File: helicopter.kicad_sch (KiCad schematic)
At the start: 15 parts, among them J1 Conn_01x06, SW1 Tactswitch, U1 STM32L4P5RET6, Y1 16MHz

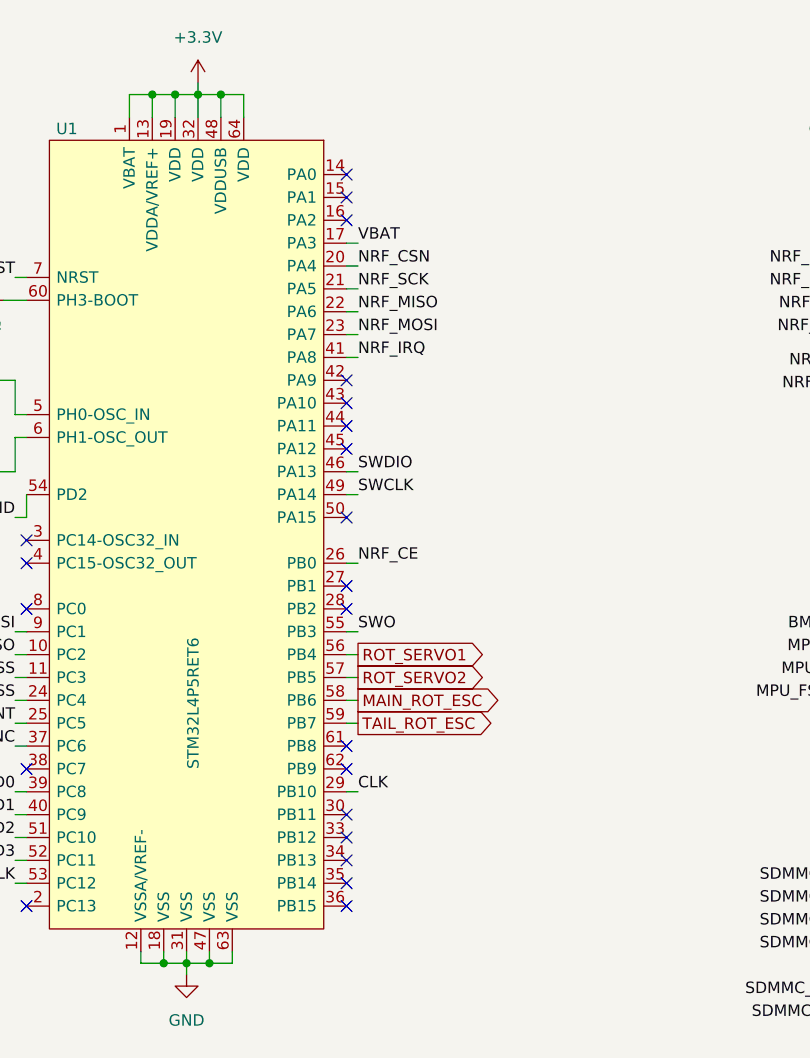
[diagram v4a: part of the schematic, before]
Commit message: Add external UART and I2C connectors
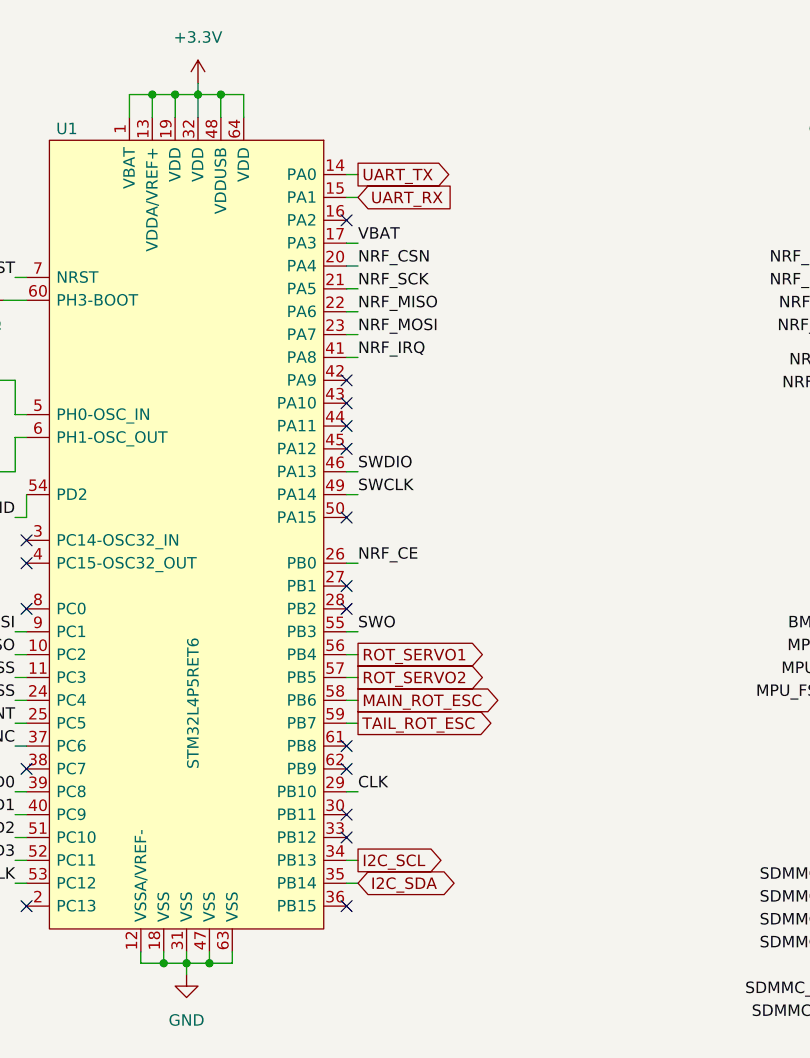
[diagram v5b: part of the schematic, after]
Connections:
- net UART_TX: now reaches U1.14 (PA0)
- net UART_RX: now reaches U1.15 (PA1)
- net I2C_SCL: now reaches U1.34 (PB13)
- net I2C_SDA: now reaches U1.35 (PB14)
- no-connect marks 22 -> 18
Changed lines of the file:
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@@
   (no_connect (at 130.81 96.52))
   (no_connect (at 166.37 81.28))
-  (no_connect (at 166.37 55.88))
   (no_connect (at 166.37 137.16))
   (no_connect (at 130.81 99.06))
   (no_connect (at 166.37 101.6))
-  (no_connect (at 166.37 58.42))
   (no_connect (at 166.37 86.36))
   (no_connect (at 166.37 129.54))
   (no_connect (at 166.37 60.96))
   (no_connect (at 130.81 137.16))
-  (no_connect (at 166.37 134.62))
   (no_connect (at 166.37 104.14))
-  (no_connect (at 166.37 132.08))
   (no_connect (at 166.37 127))
   (wire (pts (xy 107.95 78.74) (xy 111.76 78.74))
@@
     (stroke (width 0) (type default) (color 0 0 0 0))
   )
+  (wire (pts (xy 166.37 55.88) (xy 167.64 55.88))
+    (stroke (width 0) (type default) (color 0 0 0 0))
+  )
   (wire (pts (xy 76.2 128.27) (xy 67.31 128.27))
     (stroke (width 0) (type default) (color 0 0 0 0))
@@
     (stroke (width 0) (type default) (color 0 0 0 0))
   )
+  (wire (pts (xy 167.64 132.08) (xy 166.37 132.08))
+    (stroke (width 0) (type default) (color 0 0 0 0))
+  )
   (wire (pts (xy 129.54 129.54) (xy 130.81 129.54))
     (stroke (width 0) (type default) (color 0 0 0 0))
@@
     (stroke (width 0) (type default) (color 0 0 0 0))
   )
+  (wire (pts (xy 167.64 134.62) (xy 166.37 134.62))
+    (stroke (width 0) (type default) (color 0 0 0 0))
+  )
   (wire (pts (xy 251.46 44.45) (xy 252.73 44.45))
     (stroke (width 0) (type default) (color 0 0 0 0))
@@
     (stroke (width 0) (type default) (color 0 0 0 0))
   )
+  (wire (pts (xy 166.37 58.42) (xy 167.64 58.42))
+    (stroke (width 0) (type default) (color 0 0 0 0))
+  )
   (wire (pts (xy 148.59 143.51) (xy 151.13 143.51))
     (stroke (width 0) (type default) (color 0 0 0 0))
@@
   (label "MPU_FSYNC" (at 129.54 119.38 180)
     (effects (font (size 1.27 1.27)) (justify right bottom))
+  )
+  (global_label "I2C_SDA" (shape bidirectional) (at 167.64 134.62 0) (fields_autoplaced)
+    (effects (font (size 1.27 1.27)) (justify left))
+    (property "Intersheet References" "${INTERSHEET_REFS}" (id 0) (at 177.6731 134.5406 0)
+      (effects (font (size 1.27 1.27)) (justify left) hide)
+    )
+  )
+  (global_label "UART_RX" (shape input) (at 167.64 58.42 0) (fields_autoplaced)
+    (effects (font (size 1.27 1.27)) (justify left))
+    (property "Intersheet References" "${INTERSHEET_REFS}" (id 0) (at 178.1569 58.3406 0)
+      (effects (font (size 1.27 1.27)) (justify left) hide)
+    )
+  )
+  (global_label "I2C_SCL" (shape output) (at 167.64 132.08 0) (fields_autoplaced)
+    (effects (font (size 1.27 1.27)) (justify left))
+    (property "Intersheet References" "${INTERSHEET_REFS}" (id 0) (at 177.6126 132.0006 0)
+      (effects (font (size 1.27 1.27)) (justify left) hide)
+    )
+  )
+  (global_label "UART_TX" (shape output) (at 167.64 55.88 0) (fields_autoplaced)
+    (effects (font (size 1.27 1.27)) (justify left))
+    (property "Intersheet References" "${INTERSHEET_REFS}" (id 0) (at 177.8545 55.8006 0)
+      (effects (font (size 1.27 1.27)) (justify left) hide)
+    )
   )
   (global_label "ROT_SERVO2" (shape output) (at 167.64 111.76 0) (fields_autoplaced)
@@
       (reference "#PWR052") (unit 1) (value "GND") (footprint "")
     )
+    (path "/03584532-d520-432f-bf10-7b409826f4f4/e670d8e7-acb1-4d31-b7b4-7354a3ac705b"
+      (reference "#PWR053") (unit 1) (value "+3.3V") (footprint "")
+    )
     (path "/4061a02e-a9bb-43ee-a711-3c44a7f24ef0/6141ad77-e71d-4b57-9042-5d8d98bf5d20"
-      (reference "#PWR053") (unit 1) (value "+3.3V") (footprint "")
+      (reference "#PWR054") (unit 1) (value "+3.3V") (footprint "")
     )
     (path "/4061a02e-a9bb-43ee-a711-3c44a7f24ef0/6a5e99f9-d00c-409c-b5a1-dc6bd628de4a"
-      (reference "#PWR054") (unit 1) (value "GND") (footprint "")
+      (reference "#PWR055") (unit 1) (value "GND") (footprint "")
     )
     (path "/ab592a18-5785-48c5-b124-28d50fc9f6ed"
@@
       (reference "J7") (unit 1) (value "Tail Rotor ESC") (footprint "")
     )
+    (path "/03584532-d520-432f-bf10-7b409826f4f4/e9c69447-977c-4a20-ae79-3cca3335be42"
+      (reference "J8") (unit 1) (value "UART") (footprint "")
+    )
+    (path "/03584532-d520-432f-bf10-7b409826f4f4/92637023-0f95-4dac-a293-6287c2dad790"
+      (reference "J9") (unit 1) (value "I2C") (footprint "")
+    )
     (path "/8027772a-0953-4782-8447-2c100ffa6fed/8fd49e22-7d0b-4999-acfe-374e120b2804"
       (reference "L1") (unit 1) (value "2.2μH") (footprint "Inductor_SMD:L_Bourns-SRN4018")
@@
       (reference "R8") (unit 1) (value "33kΩ") (footprint "")
     )
+    (path "/03584532-d520-432f-bf10-7b409826f4f4/c80e98fc-3df3-4f97-83a2-4a272e884a21"
+      (reference "R9") (unit 1) (value "4.7kΩ") (footprint "Resistor_SMD:R_0603_1608Metric")
+    )
+    (path "/03584532-d520-432f-bf10-7b409826f4f4/d6950e8f-f3be-4e92-bc66-58d9dae0057c"
+      (reference "R10") (unit 1) (value "4.7kΩ") (footprint "Resistor_SMD:R_0603_1608Metric")
+    )
     (path "/001a8cd4-69e7-418f-926d-53dec41ad019"

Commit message: Assign footprints to symbols
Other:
- title: RC Helicopter -> RC Helicopter Mainboard
